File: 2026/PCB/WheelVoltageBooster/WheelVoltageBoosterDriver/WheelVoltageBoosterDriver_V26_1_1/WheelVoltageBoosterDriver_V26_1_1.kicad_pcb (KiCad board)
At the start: 2 copper layers, 100 x 65 mm, 194 parts, among them J1 Conn_01x02_Pin, J10 Conn_01x03_Socket, J11 Conn_01x05_Socket, J12 CAN_CON, J13 Conn_01x04_Socket, J2 Conn_01x02_Pin, J3 Conn_01x04_Socket, J4 Conn_01x04_Socket, J5 Conn_01x04_Socket, J6 Conn_01x04_Socket, J7 Conn_01x02_Pin, J8 Conn_01x07_Socket, J9 Conn_01x03_Socket, SW1 SW_MEC_5E, SW2 SW_MEC_5E, U1 MAX3051, U2 LM5170QPHPTQ1, U3 STM32H523CEU6, U4 TMP235AQDCKRQ1, U5 MAX20405AFOA/VY+, U6 LD1117DT33CTR, U7 MAX20405AFOA/VY+, Y1 Crystal_GND2

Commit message: 見えた
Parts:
- removed R43, R44: 1, Resistor_SMD:R_0402_1005Metric_Pad0.72x0.64mm_HandSolder
- added REF**: hole_M3_User, WheelVoltageBooster_LIB_FTP:hole_M3_User, F.Cu at (103.0, 124.5)
- added REF**: MountingHole_2.2mm_M2_Pad_Via, MountingHole:MountingHole_2.2mm_M2_Pad_Via, F.Cu at (110.0, 124.5)
- added REF**: hole_M3_User, WheelVoltageBooster_LIB_FTP:hole_M3_User, F.Cu at (197.0, 65.5)
- added REF**: hole_M3_User, WheelVoltageBooster_LIB_FTP:hole_M3_User, F.Cu at (197.0, 124.5)
- added REF**: MountingHole_2.2mm_M2_Pad_Via, MountingHole:MountingHole_2.2mm_M2_Pad_Via, F.Cu at (190.0, 65.5)
- added REF**: hole_M3_User, WheelVoltageBooster_LIB_FTP:hole_M3_User, F.Cu at (103.0, 65.5)
- added REF**: MountingHole_2.2mm_M2_Pad_Via, MountingHole:MountingHole_2.2mm_M2_Pad_Via, F.Cu at (190.0, 124.5)
- added REF**: MountingHole_2.2mm_M2_Pad_Via, MountingHole:MountingHole_2.2mm_M2_Pad_Via, F.Cu at (110.0, 65.5)
- J10, J3, J4, J5, J6, J9: moved to B.Cu
- moved L2 344.0 mm to (-76.9, 9.79), turned to 0 degrees
- moved C51 259.4 mm to (-33.8, -9.33)
- moved C59 233.2 mm to (-21.2, -9.33), turned to 0 degrees
- moved FET13 201.8 mm to (-18.3, 25.6), turned to 0 degrees
- moved FET10 197.5 mm to (-26.6, 25.6), turned to 0 degrees
- moved C62 195.5 mm to (-17.6, 82.3)
- moved C1 179.6 mm to (-86.3, 43.4)
- moved C10 179.6 mm to (-81.9, 43.4)
- moved C11 179.6 mm to (-81.9, 45.9)
- moved C12 179.6 mm to (-81.9, 48.4)
- moved C13 179.6 mm to (-81.9, 50.9)
- moved C14 179.6 mm to (-81.9, 53.4)
- moved C16 179.6 mm to (-81.9, 58.5)
- moved C17 179.6 mm to (-81.9, 61.0)
- moved C18 179.6 mm to (-81.9, 63.5)
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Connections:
- FET10 pad 1: Net-(FET10-S-Pad1) -> GND
- FET10 pad 2: Net-(FET10-S-Pad1) -> GND
- FET10 pad 3: Net-(FET10-S-Pad1) -> GND
- FET9 pad 1: Net-(FET9-S-Pad1) -> GND
- FET9 pad 2: Net-(FET9-S-Pad1) -> GND
- FET9 pad 3: Net-(FET9-S-Pad1) -> GND
- L1 pad 1: Net-(L1-Pad1) -> /Power_Circuit/CS2A
- L2 pad 1: Net-(L2-Pad1) -> /Power_Circuit/CS1A
- R41 pad 2: Net-(L1-Pad1) -> /Power_Circuit/CS2A
- R42 pad 2: Net-(L2-Pad1) -> /Power_Circuit/CS1A
- R49 pad 1: Net-(FET9-S-Pad1) -> GND
- R50 pad 1: Net-(FET10-S-Pad1) -> GND

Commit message: コンデンサ増殖
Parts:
- removed J12: CAN_CON, Connector_JST:JST_PH_S2B-PH-K_1x02_P2.00mm_Horizontal
- added C100: 10u, Capacitor_SMD:C_1210_3225Metric_Pad1.33x2.70mm_HandSolder, B.Cu at (113.6, 106.2)
- added C101: 10u, Capacitor_SMD:C_1210_3225Metric_Pad1.33x2.70mm_HandSolder, B.Cu at (113.6, 102.9)
- added C102: 10u, Capacitor_SMD:C_1210_3225Metric_Pad1.33x2.70mm_HandSolder, B.Cu at (113.6, 99.6)
- added C103: 10u, Capacitor_SMD:C_1210_3225Metric_Pad1.33x2.70mm_HandSolder, B.Cu at (113.6, 96.3)
- added C104: 10u, Capacitor_SMD:C_1210_3225Metric_Pad1.33x2.70mm_HandSolder, B.Cu at (143.3, 102.9)
- added C105: 10u, Capacitor_SMD:C_1210_3225Metric_Pad1.33x2.70mm_HandSolder, B.Cu at (143.3, 106.2)
- added C106: 10u, Capacitor_SMD:C_1210_3225Metric_Pad1.33x2.70mm_HandSolder, B.Cu at (156.7, 103.0)
- added C107: 10u, Capacitor_SMD:C_1210_3225Metric_Pad1.33x2.70mm_HandSolder, B.Cu at (156.7, 106.3)
- added C80: 10u, Capacitor_SMD:C_1210_3225Metric_Pad1.33x2.70mm_HandSolder, B.Cu at (193.6, 106.3)
- added C81: 10u, Capacitor_SMD:C_1210_3225Metric_Pad1.33x2.70mm_HandSolder, B.Cu at (193.6, 103.0)
- added C82: 10u, Capacitor_SMD:C_1210_3225Metric_Pad1.33x2.70mm_HandSolder, B.Cu at (193.6, 109.6)
- added C83: 10u, Capacitor_SMD:C_1210_3225Metric_Pad1.33x2.70mm_HandSolder, B.Cu at (106.4, 102.9)
- added C84: 10u, Capacitor_SMD:C_1210_3225Metric_Pad1.33x2.70mm_HandSolder, B.Cu at (106.4, 106.2)
- added C85: 10u, Capacitor_SMD:C_1210_3225Metric_Pad1.33x2.70mm_HandSolder, B.Cu at (106.4, 96.3)
- added C86: 10u, Capacitor_SMD:C_1210_3225Metric_Pad1.33x2.70mm_HandSolder, B.Cu at (106.4, 99.6)
- added C87: 10u, Capacitor_SMD:C_1210_3225Metric_Pad1.33x2.70mm_HandSolder, B.Cu at (193.6, 116.2)
- added C88: 10u, Capacitor_SMD:C_1210_3225Metric_Pad1.33x2.70mm_HandSolder, B.Cu at (193.6, 96.4)
- added C89: 10u, Capacitor_SMD:C_1210_3225Metric_Pad1.33x2.70mm_HandSolder, B.Cu at (193.6, 99.7)
- added C90: 10u, Capacitor_SMD:C_1210_3225Metric_Pad1.33x2.70mm_HandSolder, B.Cu at (186.4, 96.4)
- added C91: 10u, Capacitor_SMD:C_1210_3225Metric_Pad1.33x2.70mm_HandSolder, B.Cu at (186.4, 99.7)
- added C92: 10u, Capacitor_SMD:C_1210_3225Metric_Pad1.33x2.70mm_HandSolder, B.Cu at (186.4, 103.0)
- added C93: 10u, Capacitor_SMD:C_1210_3225Metric_Pad1.33x2.70mm_HandSolder, B.Cu at (186.4, 106.3)
- added C94: 10u, Capacitor_SMD:C_1210_3225Metric_Pad1.33x2.70mm_HandSolder, B.Cu at (186.4, 109.6)
- added C95: 10u, Capacitor_SMD:C_1210_3225Metric_Pad1.33x2.70mm_HandSolder, B.Cu at (186.4, 112.9)
- added C96: 10u, Capacitor_SMD:C_1210_3225Metric_Pad1.33x2.70mm_HandSolder, B.Cu at (186.4, 116.2)
- added C97: 10u, Capacitor_SMD:C_1210_3225Metric_Pad1.33x2.70mm_HandSolder, B.Cu at (113.6, 116.1)
- added C98: 10u, Capacitor_SMD:C_1210_3225Metric_Pad1.33x2.70mm_HandSolder, B.Cu at (113.6, 112.8)
- added C99: 10u, Capacitor_SMD:C_1210_3225Metric_Pad1.33x2.70mm_HandSolder, B.Cu at (113.6, 109.5)
- C28, C30, C32, C34, C35, C36, C37, C38, C46, C48, C52, C54, C56: value 4.7u -> 10u; footprint Capacitor_SMD:C_1206_3216Metric_Pad1.33x1.80mm_HandSolder -> Capacitor_SMD:C_1210_3225Metric_Pad1.33x2.70mm_HandSolder; moved to B.Cu
- C42, C44, C50, C58, C60: value 4.7u -> 10u; footprint Capacitor_SMD:C_1206_3216Metric_Pad1.33x1.80mm_HandSolder -> Capacitor_SMD:C_1210_3225Metric_Pad1.33x2.70mm_HandSolder
- C61: value 47u -> 10u; footprint WheelVoltageBooster_LIB_FTP:CAP_EEEFN1K470UP -> Capacitor_SMD:C_1210_3225Metric_Pad1.33x2.70mm_HandSolder
- C62: value 47u -> 10u; footprint WheelVoltageBooster_LIB_FTP:CAP_EEEFN1K470UP -> Capacitor_SMD:C_1210_3225Metric_Pad1.33x2.70mm_HandSolder; moved to B.Cu
- FET1, FET2: footprint Package_TO_SOT_SMD:TSOT-23-6_HandSoldering -> Package_TO_SOT_SMD:TSOT-23-6
- FET10, FET11, FET12, FET13, FET14, FET3, FET4, FET5, FET6, FET7, FET8, FET9: footprint Package_DFN_QFN:PQFN-8-EP_6x5mm_P1.27mm_Generic -> WheelVoltageBooster_LIB_FTP:PQFN-8-EP_6x5mm_P1.27mm_Generic_ud
- J1: footprint Connector_AMASS:AMASS_XT30PW-M_1x02_P2.50mm_Horizontal -> WheelVoltageBooster_LIB_FTP:AMASS_XT30PW-M_1x02_P2.50mm_Horizontal_ud
- R36, R37: footprint Resistor_SMD:R_0402_1005Metric_Pad0.72x0.64mm_HandSolder -> Resistor_SMD:R_0603_1608Metric_Pad0.98x0.95mm_HandSolder
- U4: footprint Package_TO_SOT_SMD:SOT-353_SC-70-5_Handsoldering -> Package_TO_SOT_SMD:SOT-353_SC-70-5
- moved FET1 274.7 mm to (189.5, 71.9), turned to -90 degrees
- moved R56 269.4 mm to (179.8, 110.8), turned to -90 degrees
- moved R55 268.2 mm to (179.8, 104.9), turned to -90 degrees
- moved L2 265.6 mm to (176.3, 89.8)
- moved R46 263.3 mm to (169.4, 110.8), turned to -90 degrees
- moved J2 262.7 mm to (193.1, 72.9), turned to 90 degrees
- moved R50 260.2 mm to (169.4, 104.9), turned to -90 degrees
- moved C47 259.0 mm to (193.6, 107.7)
- moved C43 256.5 mm to (193.6, 81.0)
- moved R18 254.2 mm to (188.0, 69.3), turned to 180 degrees
- moved R19 254.1 mm to (188.0, 74.4)
- moved C55 251.0 mm to (193.6, 116.6)
- moved C58 248.5 mm to (180.6, 115.3), turned to 90 degrees
- moved C51 248.1 mm to (193.6, 89.9)
- moved C60 244.2 mm to (177.3, 115.3), turned to 90 degrees
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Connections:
- C46 pad 1: +50V -> +20V
- C48 pad 1: +50V -> +20V

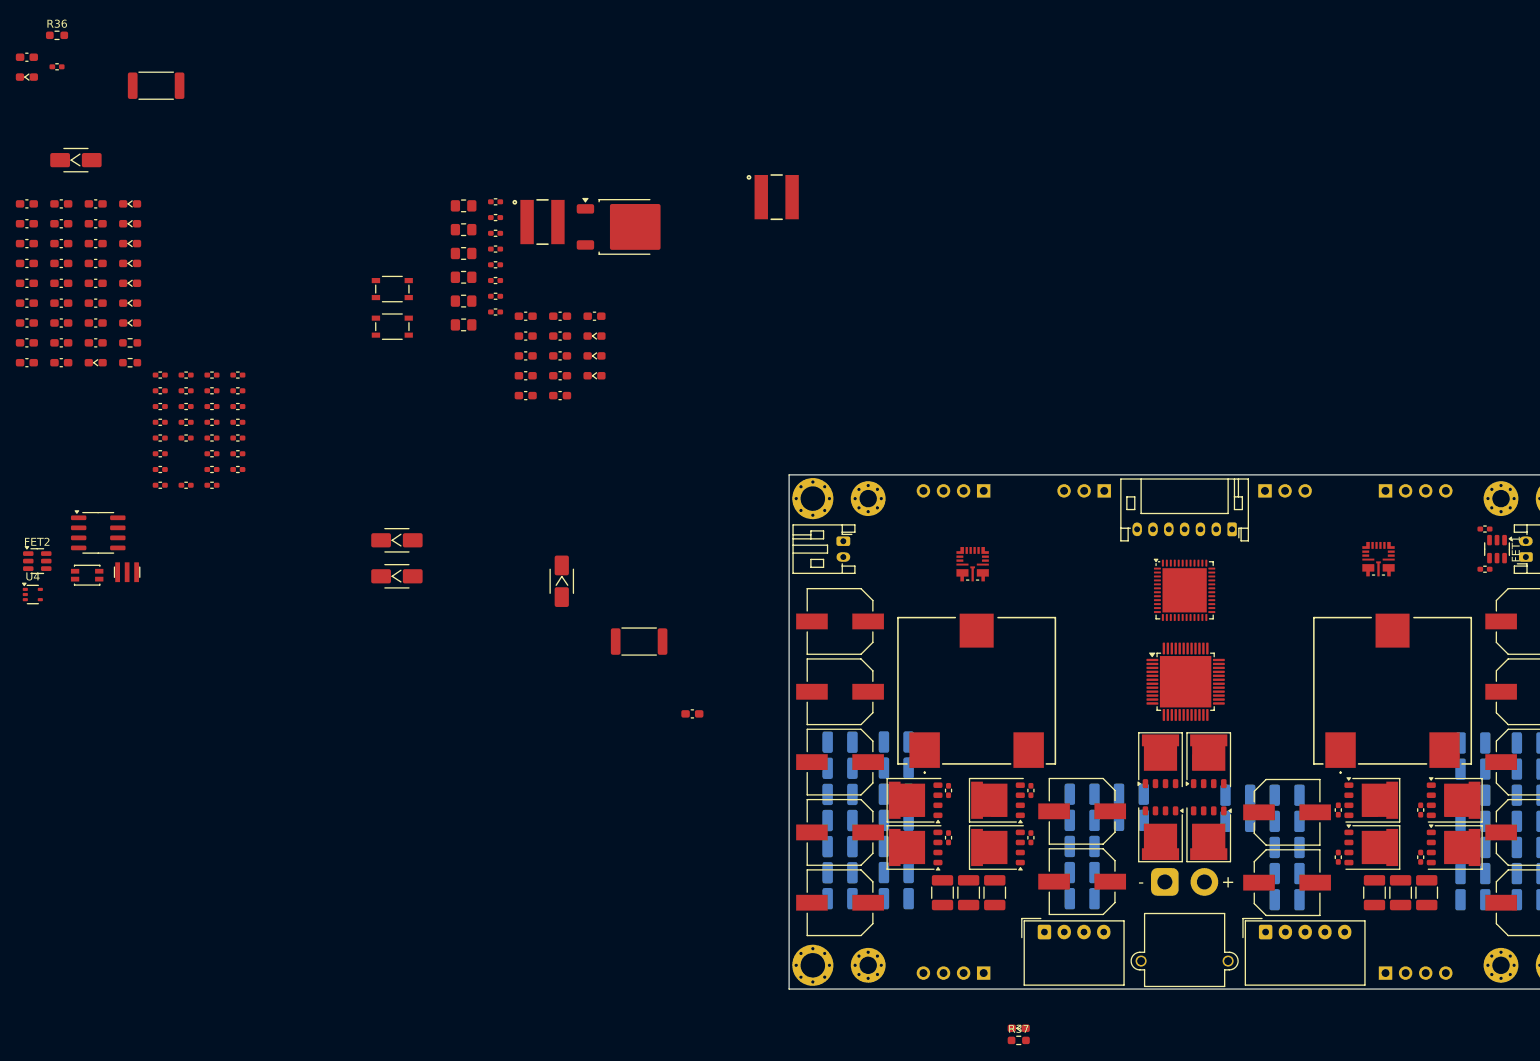
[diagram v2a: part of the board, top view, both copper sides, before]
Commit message: Bias系統を配置
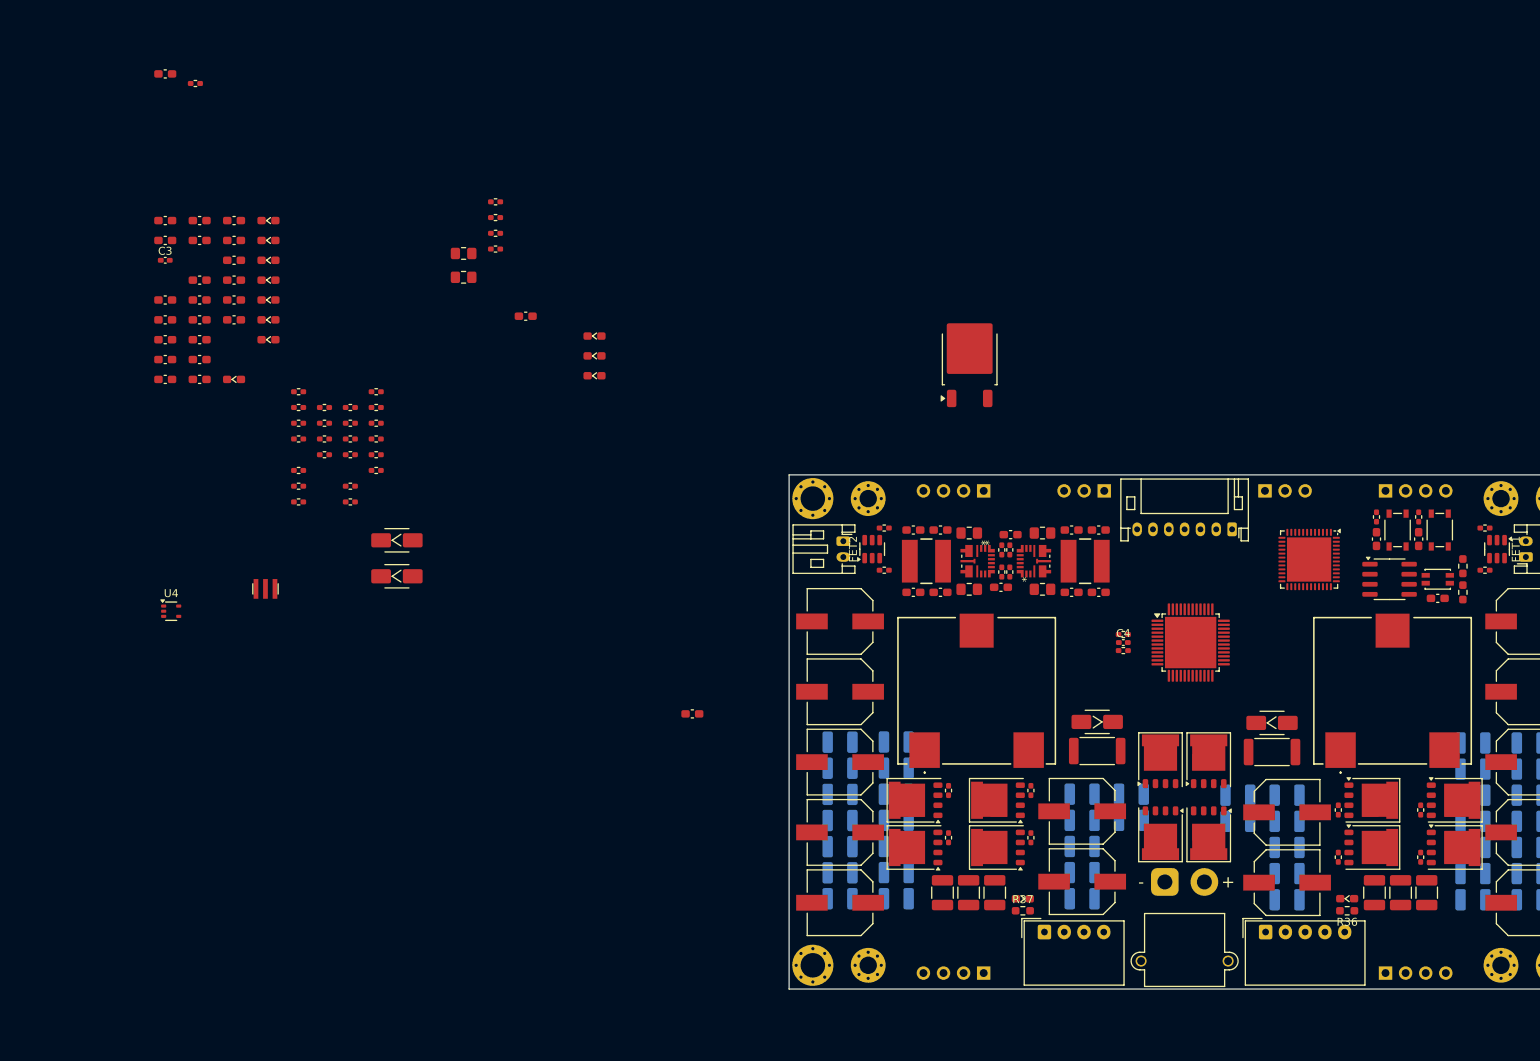
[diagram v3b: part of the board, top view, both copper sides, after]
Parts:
- C3, C4: footprint Capacitor_SMD:C_0603_1608Metric_Pad1.08x0.95mm_HandSolder -> Capacitor_SMD:C_0402_1005Metric_Pad0.74x0.62mm_HandSolder
- moved R36 197.1 mm to (170.6, 117.6), turned to 180 degrees
- moved D11 196.6 mm to (170.6, 116.1)
- moved C12 179.7 mm to (182.0, 78.1), turned to 180 degrees
- moved R13 171.0 mm to (185.2, 77.3), turned to -90 degrees
- moved R12 170.8 mm to (185.2, 74.0), turned to 90 degrees
- moved FL1 170.7 mm to (182.0, 75.7)
- moved C25 169.5 mm to (179.6, 70.6), turned to -90 degrees
- moved D14 167.1 mm to (161.0, 93.9)
- moved R42 164.3 mm to (161.0, 97.5)
- moved C26 163.8 mm to (174.3, 70.6), turned to -90 degrees
- moved U1 163.4 mm to (175.9, 75.7)
- moved R26 152.8 mm to (179.6, 67.8), turned to -90 degrees
- moved C4 146.7 mm to (142.3, 83.7)
- moved R35 144.1 mm to (174.3, 67.8), turned to -90 degrees
- moved SW1 135.9 mm to (182.3, 69.5), turned to -90 degrees
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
